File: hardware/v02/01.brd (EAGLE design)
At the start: 93.7 x 43.8 mm, 30 parts, among them IC1 MSP430G2553, IC2 78L05Z, X2 RJ45-6L-B

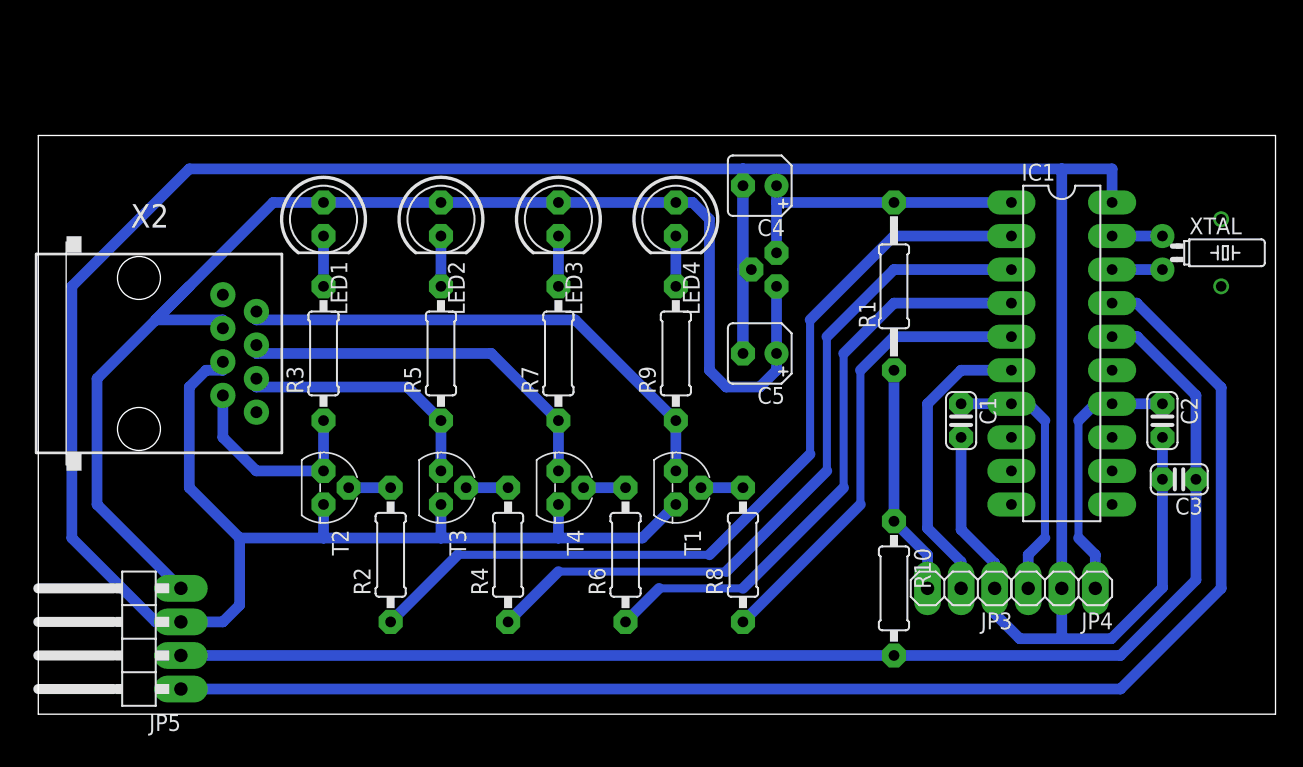
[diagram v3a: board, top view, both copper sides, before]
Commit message: rearranged transistorsand LEDs; additional resistors; pre final version
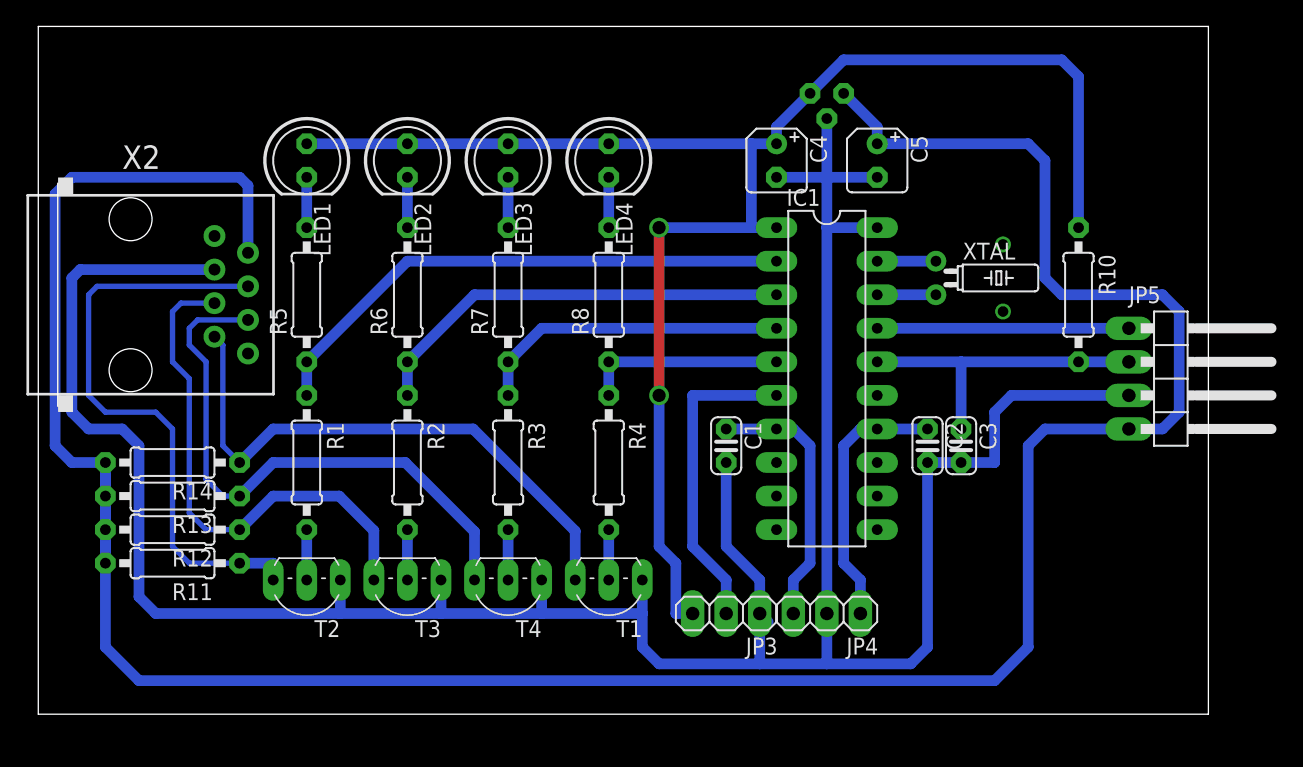
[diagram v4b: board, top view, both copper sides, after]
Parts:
- removed R9: 220, rcl:0207/10
- added R11, R12, R13, R14: 10k, rcl:0207/10
- R1: value 0 -> 470; device rcl:0207/12 -> rcl:0207/10
- R3: value 220 -> 470
- R6, R8: value 470 -> 220
- T1, T2, T3, T4: device transistor:TO92 -> transistor:TO92-EBC
- moved JP5 81.8 mm to (86.4, 25.4), turned to 270 degrees
- moved R1 46.4 mm to (20.3, 19.1), turned to 270 degrees
- moved R10 26.3 mm to (78.7, 31.8)
- moved R6 25.7 mm to (27.9, 31.8)
- moved R8 22.2 mm to (43.2, 31.8)
- moved C2 17.9 mm to (67.3, 20.3)
- moved IC1 17.9 mm to (59.7, 25.4)
- moved JP4 17.9 mm to (59.7, 7.62)
- moved C1 17.9 mm to (52.1, 20.3)
- moved JP3 17.9 mm to (52.1, 7.62)
- moved XTAL 17.3 mm to (67.9, 33.0)
- moved C5 17.1 mm to (63.5, 41.9), turned to 270 degrees
- moved C3 16.7 mm to (69.8, 20.3), turned to 270 degrees
- moved R3 16.2 mm to (35.6, 19.1), turned to 270 degrees
- moved IC2 13.9 mm to (59.7, 47.0), turned to 180 degrees
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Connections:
- removed net N$10: R9.1, T1.3, X2.2
- removed net N$14: R3.1, T2.3, X2.7
- removed net N$15: JP3.3, R1.1, R10.1
- removed net N$19: R5.1, T3.3, X2.6
- removed net N$22: R7.1, T4.3, X2.4
- new net N$27: R14.1, T1.C, X2.7
- new net N$28: R13.1, T4.C, X2.6
- new net N$29: R12.1, T3.C, X2.5
- new net N$30: R11.1, T2.C, X2.4
- net +5V: now also R11.2, R12.2, R13.2, R14.2, X2.2; no longer LED1.A, LED2.A, LED3.A, LED4.A, X2.3
- net GND: now also T1.E, T2.E, T3.E, T4.E, X2.3; no longer T1.1, T2.1, T3.1, T4.1, X2.5
- net N$11: now also R4.2, T1.B; no longer R8.2, T1.2
- net N$12: now also R1.1, R5.1; no longer R2.1
- net N$13: now also R5.2; no longer R3.2
- net N$16: now also R1.2, T2.B; no longer R2.2, T2.2
- net N$17: now also R6.2; no longer R5.2
- net N$20: now also R2.2, T3.B; no longer R4.2, T3.2
- net N$23: now also R3.2, T4.B; no longer R6.2, T4.2
- net N$8: now also R8.2; no longer R9.2
- net N$9: now also R2.1, R6.1; no longer R4.1
- net PB: now also R4.1
- net PR: now also R3.1, R7.1; no longer R6.1
- net VCC: now also JP3.3, LED1.A, LED2.A, LED3.A, LED4.A, R10.1; no longer R1.2
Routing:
- net +5V: track 104.1 -> 210.9 mm
- net VCC: track 22.9 -> 120.0 mm, vias 0 -> 2
- net N$6: track 108.0 -> 19.0 mm
- net N$5: track 101.4 -> 24.1 mm
- net GND: track 287.7 -> 216.2 mm
- net N$30: track 0.00 -> 45.7 mm
- net N$28: track 0.00 -> 44.4 mm
- net N$27: track 0.00 -> 43.7 mm
- net N$29: track 0.00 -> 39.6 mm
- net N$10: track 39.4 -> 0.00 mm
- net N$22: track 29.4 -> 0.00 mm
- net N$12: track 65.0 -> 41.3 mm
- net N$9: track 55.1 -> 32.6 mm
- net PR: track 45.2 -> 23.9 mm
- net PB: track 35.2 -> 15.2 mm
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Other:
- board size 93.7 x 43.8 mm -> 88.6 x 52.1 mm
